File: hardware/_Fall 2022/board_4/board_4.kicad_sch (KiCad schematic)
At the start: 11 parts, among them J1 Conn_01x04, J2 Conn_01x02, J3 Conn_01x07, U1 Teensy4.1

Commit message: Add new connector
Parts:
- added J?: Conn_01x21, symbol Connector_Generic:Conn_01x21
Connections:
- net CS: no longer J1.1 (Pin_1)
- net GND: no longer J2.2 (Pin_2)
- net MISO 0: no longer J1.3 (Pin_3)
- net MOSI 0: no longer J1.2 (Pin_2)
- net SCK 0: no longer J1.4 (Pin_4)
- net V_TEENSY: no longer J2.1 (Pin_1)
- net SDA 1: now reaches U1.40 (18_A4_SDA)
- net SCL 1: now reaches U1.41 (19_A5_SCL)
- no-connect marks 52 -> 50
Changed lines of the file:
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@@
   (no_connect (at 231.14 111.76))
   (no_connect (at 231.14 44.45))
-  (no_connect (at 231.14 59.69))
   (no_connect (at 231.14 106.68))
   (no_connect (at 175.26 49.53))
@@
   (no_connect (at 175.26 52.07))
   (no_connect (at 175.26 41.91))
-  (no_connect (at 231.14 57.15))
   (no_connect (at 231.14 109.22))
   (no_connect (at 231.14 116.84))
@@
     (stroke (width 0) (type default) (color 0 0 0 0))
   )
-  (wire (pts (xy 110.49 35.56) (xy 120.65 35.56))
+  (wire (pts (xy 76.2 39.37) (xy 86.36 39.37))
     (stroke (width 0) (type default) (color 0 0 0 0))
   )
@@
     (stroke (width 0) (type default) (color 0 0 0 0))
   )
+  (wire (pts (xy 231.14 57.15) (xy 234.95 57.15))
+    (stroke (width 0) (type default) (color 0 0 0 0))
+  )
   (wire (pts (xy 162.56 62.23) (xy 175.26 62.23))
     (stroke (width 0) (type default) (color 0 0 0 0))
@@
     (stroke (width 0) (type default) (color 0 0 0 0))
   )
+  (wire (pts (xy 76.2 36.83) (xy 86.36 36.83))
+    (stroke (width 0) (type default) (color 0 0 0 0))
+  )
   (wire (pts (xy 264.16 36.83) (xy 264.16 43.18))
     (stroke (width 0) (type default) (color 0 0 0 0))
@@
     (stroke (width 0) (type default) (color 0 0 0 0))
   )
-  (wire (pts (xy 110.49 38.1) (xy 120.65 38.1))
+  (wire (pts (xy 76.2 34.29) (xy 86.36 34.29))
     (stroke (width 0) (type default) (color 0 0 0 0))
   )
@@
     (stroke (width 0) (type default) (color 0 0 0 0))
   )
+  (wire (pts (xy 76.2 31.75) (xy 86.36 31.75))
+    (stroke (width 0) (type default) (color 0 0 0 0))
+  )
+  (wire (pts (xy 76.2 29.21) (xy 86.36 29.21))
+    (stroke (width 0) (type default) (color 0 0 0 0))
+  )
   (wire (pts (xy 114.3 128.27) (xy 121.92 128.27))
     (stroke (width 0) (type default) (color 0 0 0 0))
@@
     (stroke (width 0) (type default) (color 0 0 0 0))
   )
-  (wire (pts (xy 110.49 52.07) (xy 120.65 52.07))
-    (stroke (width 0) (type default) (color 0 0 0 0))
-  )
   (wire (pts (xy 114.3 116.84) (xy 121.92 116.84))
     (stroke (width 0) (type default) (color 0 0 0 0))
@@
     (stroke (width 0) (type default) (color 0 0 0 0))
   )
+  (wire (pts (xy 231.14 59.69) (xy 234.95 59.69))
+    (stroke (width 0) (type default) (color 0 0 0 0))
+  )
+  (wire (pts (xy 76.2 44.45) (xy 86.36 44.45))
+    (stroke (width 0) (type default) (color 0 0 0 0))
+  )
+  (wire (pts (xy 76.2 41.91) (xy 86.36 41.91))
+    (stroke (width 0) (type default) (color 0 0 0 0))
+  )
   (wire (pts (xy 129.54 128.27) (xy 143.51 128.27))
     (stroke (width 0) (type default) (color 0 0 0 0))
@@
     (stroke (width 0) (type default) (color 0 0 0 0))
   )
+  (wire (pts (xy 76.2 26.67) (xy 86.36 26.67))
+    (stroke (width 0) (type default) (color 0 0 0 0))
+  )
   (wire (pts (xy 162.56 82.55) (xy 175.26 82.55))
     (stroke (width 0) (type default) (color 0 0 0 0))
@@
     (stroke (width 0) (type default) (color 0 0 0 0))
   )
-  (wire (pts (xy 110.49 43.18) (xy 120.65 43.18))
-    (stroke (width 0) (type default) (color 0 0 0 0))
-  )
-  (wire (pts (xy 110.49 54.61) (xy 120.65 54.61))
-    (stroke (width 0) (type default) (color 0 0 0 0))
-  )
   (wire (pts (xy 264.16 77.47) (xy 264.16 88.9))
     (stroke (width 0) (type default) (color 0 0 0 0))
@@
     (stroke (width 0) (type default) (color 0 0 0 0))
   )
-  (wire (pts (xy 110.49 40.64) (xy 120.65 40.64))
-    (stroke (width 0) (type default) (color 0 0 0 0))
-  )
   (wire (pts (xy 110.49 72.39) (xy 120.65 72.39))
     (stroke (width 0) (type default) (color 0 0 0 0))
@@
     (effects (font (size 1.27 1.27)) (justify left bottom))
   )
-  (label "MISO 0" (at 110.49 40.64 0)
+  (label "TX 2" (at 76.2 54.61 0)
+    (effects (font (size 1.27 1.27)) (justify left bottom))
+  )
+  (label "RX 3" (at 76.2 57.15 0)
+    (effects (font (size 1.27 1.27)) (justify left bottom))
+  )
+  (label "TX 4" (at 76.2 64.77 0)
+    (effects (font (size 1.27 1.27)) (justify left bottom))
+  )
+  (label "RX 5" (at 76.2 67.31 0)
     (effects (font (size 1.27 1.27)) (justify left bottom))
   )
@@
     (effects (font (size 1.27 1.27)) (justify left bottom))
   )
-  (label "MOSI 0" (at 110.49 38.1 0)
+  (label "MOSI 0" (at 76.2 34.29 0)
+    (effects (font (size 1.27 1.27)) (justify left bottom))
+  )
+  (label "SDA 1" (at 76.2 44.45 0)
     (effects (font (size 1.27 1.27)) (justify left bottom))
   )
@@
     (effects (font (size 1.27 1.27)) (justify left bottom))
   )
+  (label "RX 8" (at 76.2 82.55 0)
+    (effects (font (size 1.27 1.27)) (justify left bottom))
+  )
   (label "MISO 0" (at 162.56 72.39 0)
     (effects (font (size 1.27 1.27)) (justify left bottom))
@@
     (effects (font (size 1.27 1.27)) (justify left bottom))
   )
-  (label "V_TEENSY" (at 110.49 52.07 0)
+  (label "TX 6" (at 76.2 74.93 0)
+    (effects (font (size 1.27 1.27)) (justify left bottom))
+  )
+  (label "SCK 0" (at 76.2 39.37 0)
     (effects (font (size 1.27 1.27)) (justify left bottom))
   )
@@
     (effects (font (size 1.27 1.27)) (justify left bottom))
   )
+  (label "TX 3" (at 76.2 59.69 0)
+    (effects (font (size 1.27 1.27)) (justify left bottom))
+  )
+  (label "CS" (at 76.2 31.75 0)
+    (effects (font (size 1.27 1.27)) (justify left bottom))
+  )
   (label "V_TEENSY" (at 264.16 36.83 0)
     (effects (font (size 1.27 1.27)) (justify left bottom))
   )
-  (label "CS" (at 110.49 35.56 0)
-    (effects (font (size 1.27 1.27)) (justify left bottom))
-  )
   (label "V_TEENSY" (at 240.03 39.37 0)
     (effects (font (size 1.27 1.27)) (justify left bottom))
   )
+  (label "SDA 1" (at 234.95 59.69 0)
+    (effects (font (size 1.27 1.27)) (justify left bottom))
+  )
+  (label "5 V" (at 43.18 86.36 0)
+    (effects (font (size 1.27 1.27)) (justify left bottom))
+  )
+  (label "V_TEENSY" (at 76.2 26.67 0)
+    (effects (font (size 1.27 1.27)) (justify left bottom))
+  )
   (label "CS" (at 162.56 67.31 0)
     (effects (font (size 1.27 1.27)) (justify left bottom))
   )
+  (label "RX 1" (at 76.2 46.99 0)
+    (effects (font (size 1.27 1.27)) (justify left bottom))
+  )
+  (label "3.3 V" (at 43.18 83.82 0)
+    (effects (font (size 1.27 1.27)) (justify left bottom))
+  )
   (label "GND" (at 264.16 58.42 0)
     (effects (font (size 1.27 1.27)) (justify left bottom))
   )
+  (label "MISO 0" (at 76.2 36.83 0)
+    (effects (font (size 1.27 1.27)) (justify left bottom))
+  )
   (label "MOSI 2" (at 162.56 87.63 0)
     (effects (font (size 1.27 1.27)) (justify left bottom))
@@
     (effects (font (size 1.27 1.27)) (justify left bottom))
   )
+  (label "RX 6" (at 76.2 72.39 0)
+    (effects (font (size 1.27 1.27)) (justify left bottom))
+  )
+  (label "TX 8" (at 76.2 85.09 0)
+    (effects (font (size 1.27 1.27)) (justify left bottom))
+  )
   (label "MOSI 0" (at 162.56 69.85 0)
     (effects (font (size 1.27 1.27)) (justify left bottom))
@@
     (effects (font (size 1.27 1.27)) (justify left bottom))
   )
+  (label "SCL 1" (at 234.95 57.15 0)
+    (effects (font (size 1.27 1.27)) (justify left bottom))
+  )
+  (label "GND" (at 76.2 29.21 0)
+    (effects (font (size 1.27 1.27)) (justify left bottom))
+  )
+  (label "RX 2" (at 76.2 52.07 0)
+    (effects (font (size 1.27 1.27)) (justify left bottom))
+  )
   (label "LED 2" (at 143.51 116.84 0)
     (effects (font (size 1.27 1.27)) (justify left bottom))
   )
+  (label "RX 7" (at 76.2 77.47 0)
+    (effects (font (size 1.27 1.27)) (justify left bottom))
+  )
   (label "MISO 1" (at 110.49 64.77 0)
     (effects (font (size 1.27 1.27)) (justify left bottom))
   )
+  (label "TX 5" (at 76.2 69.85 0)
+    (effects (font (size 1.27 1.27)) (justify left bottom))
+  )
+  (label "RX 4" (at 76.2 62.23 0)
+    (effects (font (size 1.27 1.27)) (justify left bottom))
+  )
   (label "SCK 2" (at 110.49 72.39 0)
     (effects (font (size 1.27 1.27)) (justify left bottom))
   )
-  (label "GND" (at 110.49 54.61 0)
+  (label "GND" (at 43.18 81.28 0)
+    (effects (font (size 1.27 1.27)) (justify left bottom))
+  )
+  (label "TX 1" (at 76.2 49.53 0)
     (effects (font (size 1.27 1.27)) (justify left bottom))
   )
@@
     (effects (font (size 1.27 1.27)) (justify left bottom))
   )
-  (label "SCK 0" (at 110.49 43.18 0)
+  (label "TX 7" (at 76.2 80.01 0)
+    (effects (font (size 1.27 1.27)) (justify left bottom))
+  )
+  (label "SCL 1" (at 76.2 41.91 0)
     (effects (font (size 1.27 1.27)) (justify left bottom))
   )
@@
     (pin "1")
     (pin "2")
+  )
+  (symbol (lib_id "Connector_Generic:Conn_01x21") (at 58.42 60.96 0) (unit 1)
+    (in_bom yes) (on_board yes) (fields_autoplaced)
+    (property "Reference" "J?" (id 0) (at 60.96 59.6899 0)
+      (effects (font (size 1.27 1.27)) (justify left))
+    )
+    (property "Value" "Conn_01x21" (id 1) (at 60.96 62.2299 0)
+      (effects (font (size 1.27 1.27)) (justify left))
+    )
+    (property "Footprint" "" (id 2) (at 58.42 60.96 0)
+      (effects (font (size 1.27 1.27)) hide)
+    )
+    (property "Datasheet" "~" (id 3) (at 58.42 60.96 0)
+      (effects (font (size 1.27 1.27)) hide)
+    )
+    (pin "1")
+    (pin "10")
+    (pin "11")
+    (pin "12")
+    (pin "13")
+    (pin "14")
+    (pin "15")
+    (pin "16")
+    (pin "17")
+    (pin "18")
+    (pin "19")
+    (pin "2")
+    (pin "20")
+    (pin "21")
+    (pin "3")
+    (pin "4")
+    (pin "5")
+    (pin "6")
+    (pin "7")
+    (pin "8")
+    (pin "9")
   )
   (symbol (lib_id "Connector_Generic:Conn_01x07") (at 125.73 69.85 0) (unit 1)
@@
       (reference "J3") (unit 1) (value "Conn_01x07") (footprint "")
     )
+    (path "/97f12cb7-29c1-4cb0-8822-40a5f379b0ce"
+      (reference "J?") (unit 1) (value "Conn_01x21") (footprint "")
+    )
     (path "/e655f3b3-e993-4244-95f7-b84bf5f4db23"

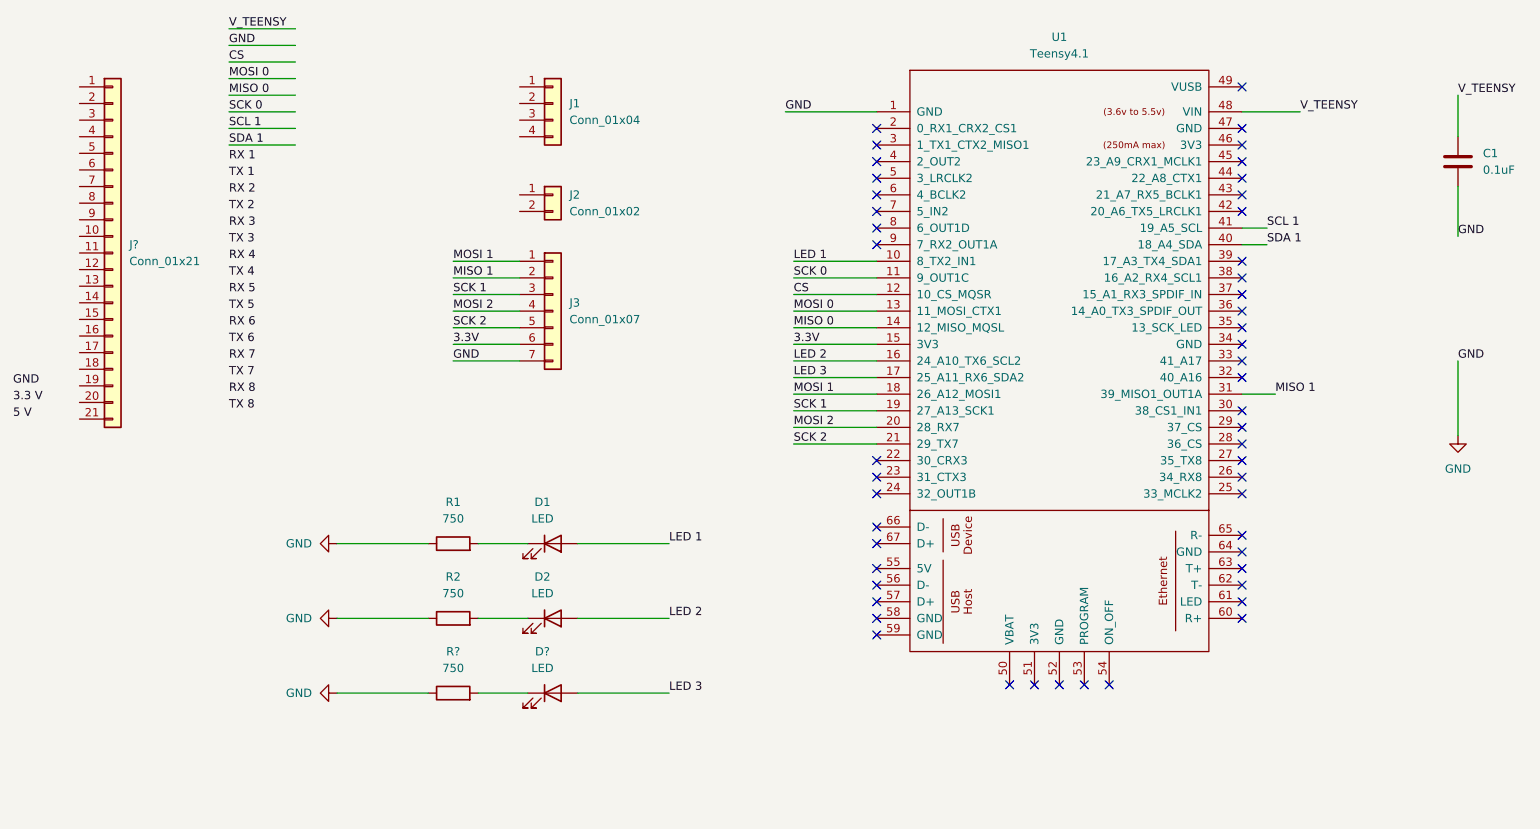
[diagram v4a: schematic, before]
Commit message: Update now teensy connection
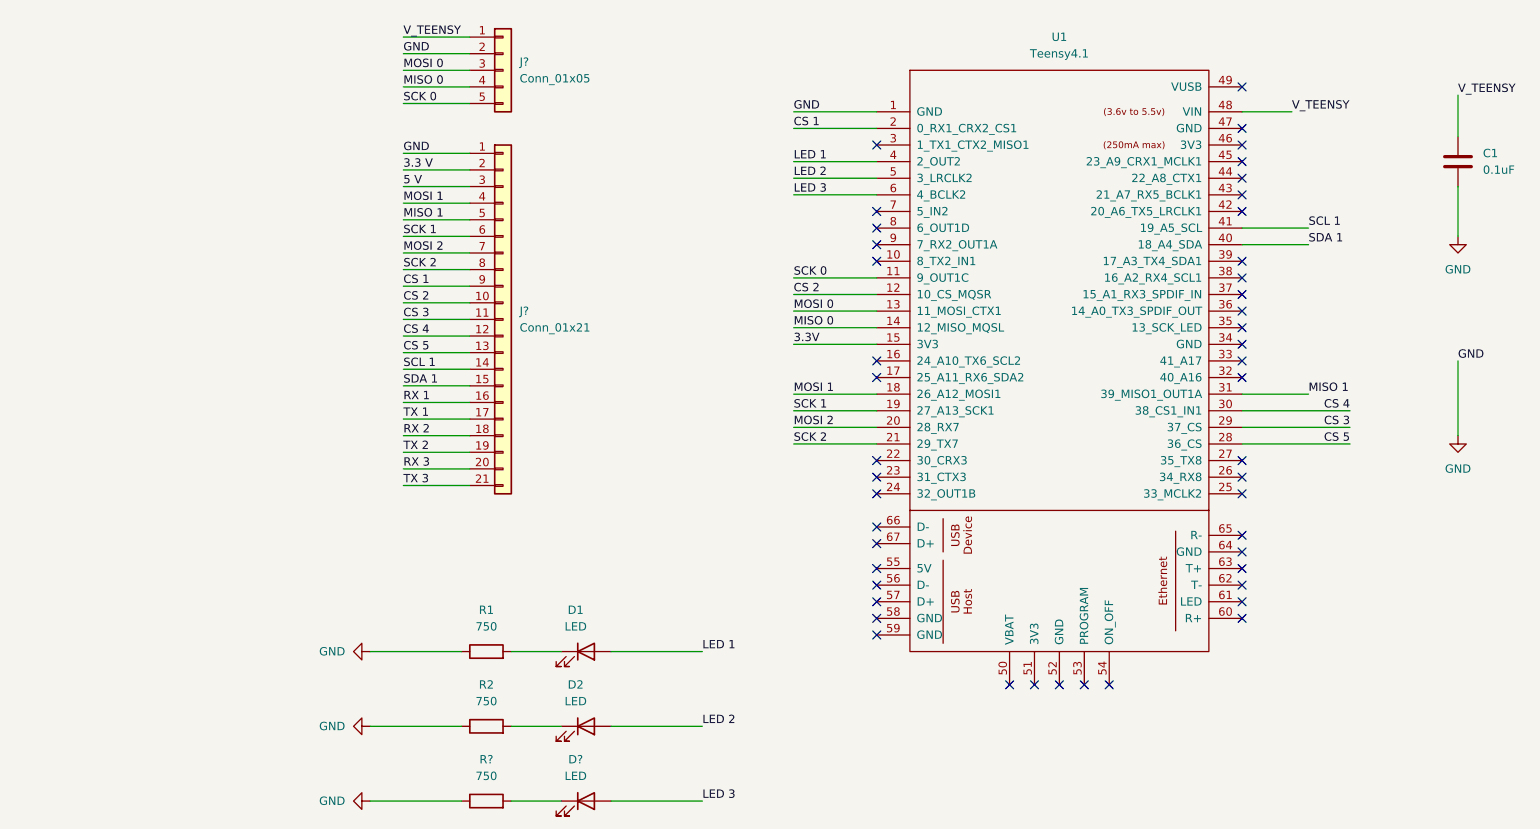
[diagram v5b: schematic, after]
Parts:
- removed J1: Conn_01x04, symbol Connector_Generic:Conn_01x04
- removed J2: Conn_01x02, symbol Connector_Generic:Conn_01x02
- removed J3: Conn_01x07, symbol Connector_Generic:Conn_01x07
- added J?: Conn_01x05, symbol Connector_Generic:Conn_01x05
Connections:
- net CS is gone; now on net CS 2: U1.12 (10_CS_MQSR)
- net 3.3 V: now also J?.2 (Pin_2)
- net 5 V: now also J?.3 (Pin_3)
- net GND: now also J?.1 (Pin_1), J?.2 (Pin_2)
- net LED 1: now also U1.4 (2_OUT2); no longer U1.10 (8_TX2_IN1)
- net LED 2: now also U1.5 (3_LRCLK2); no longer U1.16 (24_A10_TX6_SCL2)
- net LED 3: now also U1.6 (4_BCLK2); no longer U1.17 (25_A11_RX6_SDA2)
- net MISO 0: now also J?.4 (Pin_4)
- net MISO 1: now also J?.5 (Pin_5)
- net MOSI 0: now also J?.3 (Pin_3)
- net MOSI 1: now also J?.4 (Pin_4)
- net MOSI 2: now also J?.7 (Pin_7)
- net RX 1: now also J?.16 (Pin_16)
- net RX 2: now also J?.18 (Pin_18)
- net RX 3: now also J?.20 (Pin_20)
- net SCK 0: now also J?.5 (Pin_5)
- net SCK 1: now also J?.6 (Pin_6)
- net SCK 2: now also J?.8 (Pin_8)
- net SCL 1: now also J?.14 (Pin_14)
- net SDA 1: now also J?.15 (Pin_15)
- net TX 1: now also J?.17 (Pin_17)
- net TX 2: now also J?.19 (Pin_19)
- net TX 3: now also J?.21 (Pin_21)
- net V_TEENSY: now also J?.1 (Pin_1)
- net CS 2: now reaches J?.10 (Pin_10)
- net CS 3: now reaches J?.11 (Pin_11)
- net CS 3: now also U1.29 (37_CS)
- net CS 4: now reaches J?.12 (Pin_12)
- net CS 4: now also U1.30 (38_CS1_IN1)
- net CS 5: now reaches J?.13 (Pin_13)
- net CS 5: now also U1.28 (36_CS)
- net CS 1: now reaches J?.9 (Pin_9)
- net CS 1: now also U1.2 (0_RX1_CRX2_CS1)
- no-connect marks 50 -> 46
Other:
- moved on the sheet: D1, D2, D?, J?, R1, R2, R?
